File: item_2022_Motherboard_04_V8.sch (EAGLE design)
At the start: 127 parts, among them IC1 MCP602SN, IC2 LD117AS33TR, IC3 MCP1525TO, IC4 MCP6S26, IC5 MCP6004SO, IC6 MCP6004SO, IC7 MCP3204SL, IC8 LM336LP, IC9 MCP6004SO, U1 ESP32-DEVKITC-32D, U2 ADS1256_BOARD, U3 SSD1306_128X64, X1 MSTBA4, X2 MSTBA4

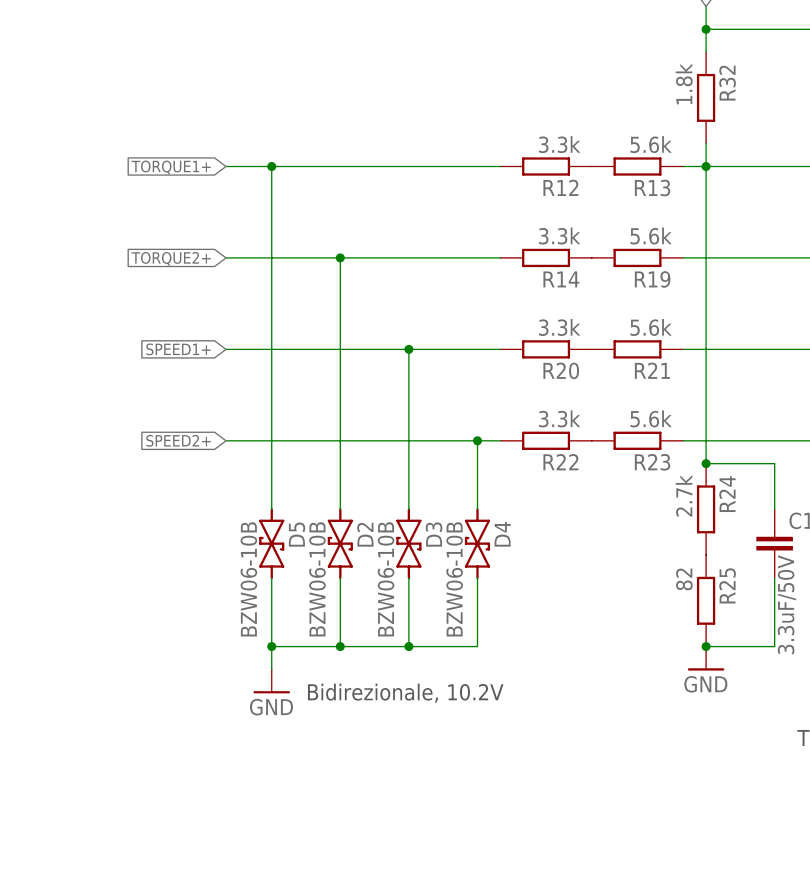
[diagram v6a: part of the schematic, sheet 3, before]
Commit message: spostati BZW su Frontend da motherboard
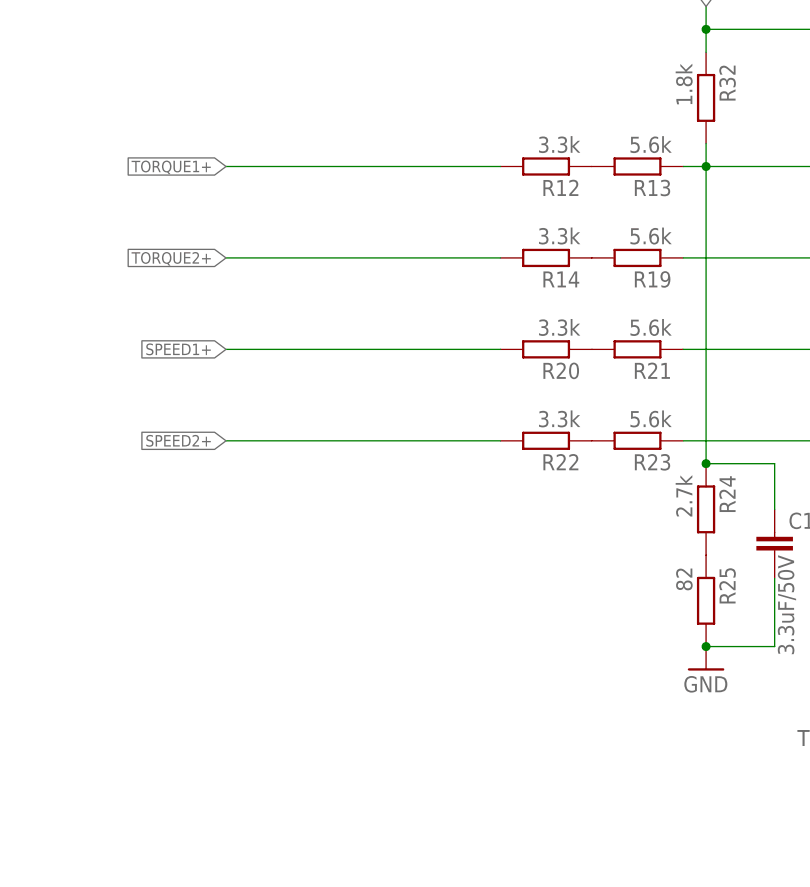
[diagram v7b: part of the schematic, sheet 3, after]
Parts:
- removed D2, D3, D4, D5: BZW06-10B, diode_LargePads:BZW04XXB
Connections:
- net GND: no longer D2.2, D3.2, D4.2, D5.2
- net SPEED1+: no longer D3.1
- net SPEED2+: no longer D4.1
- net TORQUE1+: no longer D5.1
- net TORQUE2+: no longer D2.1
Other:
- note removed: "Bidirezionale, 10.2V"

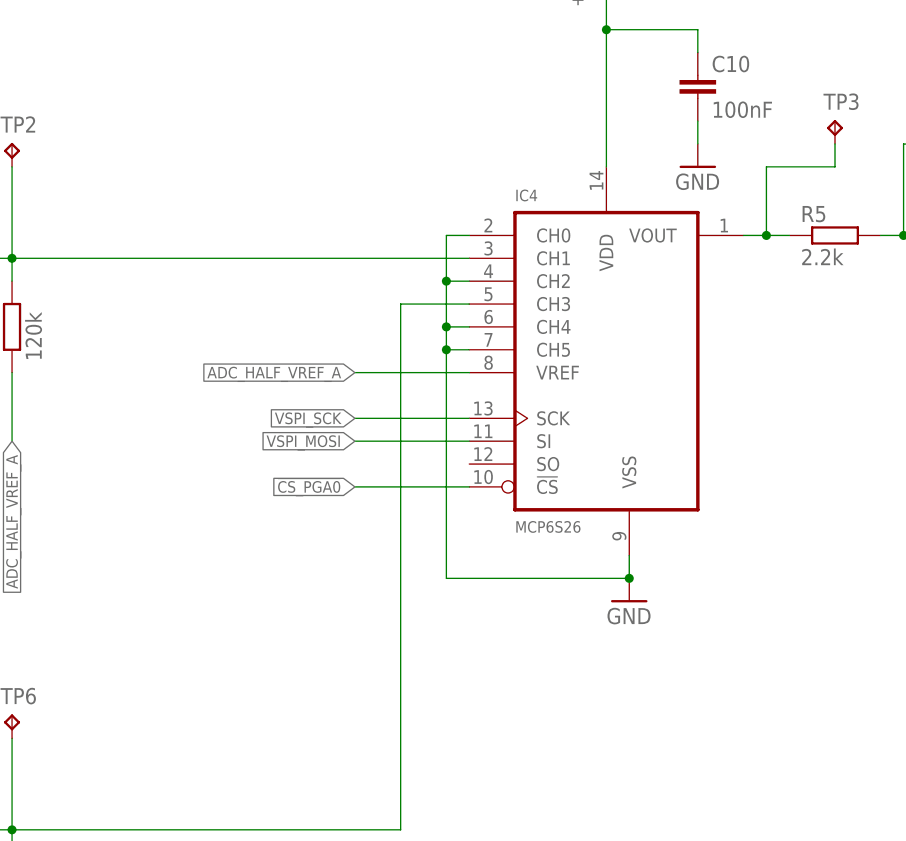
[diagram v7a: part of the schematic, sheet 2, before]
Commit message: MCP6S28 DIL
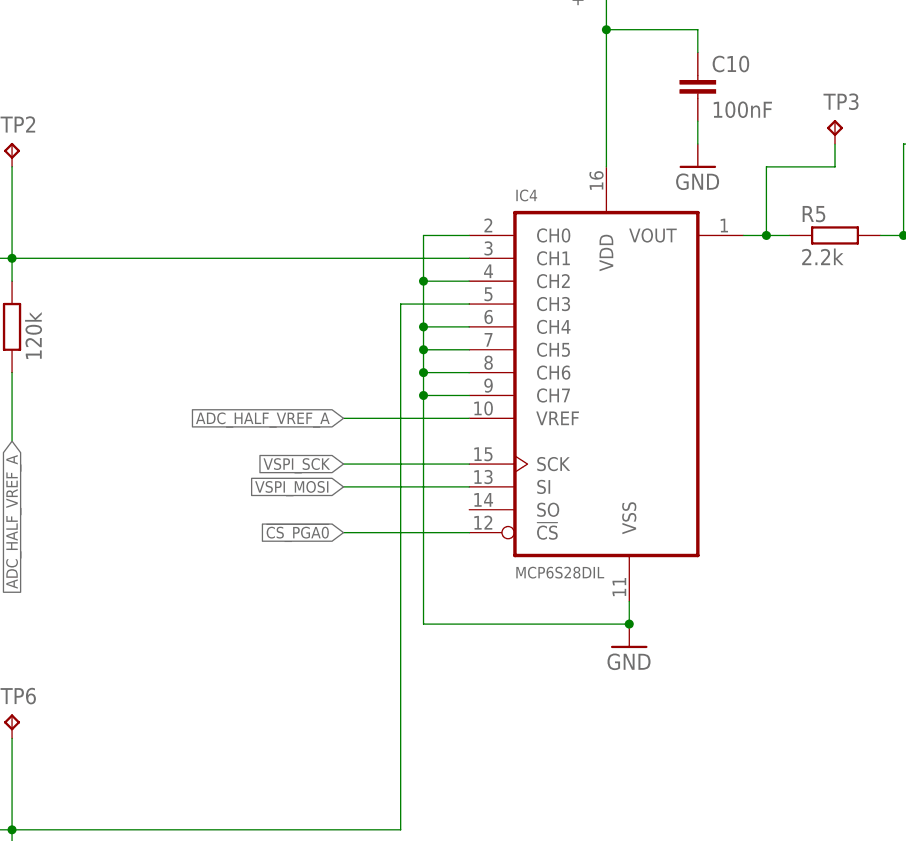
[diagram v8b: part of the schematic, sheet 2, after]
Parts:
- IC4: value MCP6S26 -> MCP6S28DIL; device microchip_opamp:MCP6S26 -> microchip_opamp:MCP6S28DIL
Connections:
- net GND: now also IC4.CH6, IC4.CH7
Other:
- moved on the sheet: U3
